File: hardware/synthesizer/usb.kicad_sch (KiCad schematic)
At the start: 6 parts, among them J8 USB_C_Receptacle_USB2.0_14P, U6 USBLC6-2P6

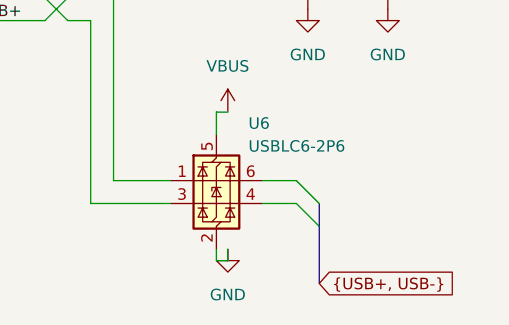
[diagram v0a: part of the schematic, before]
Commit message: start connecting sheets
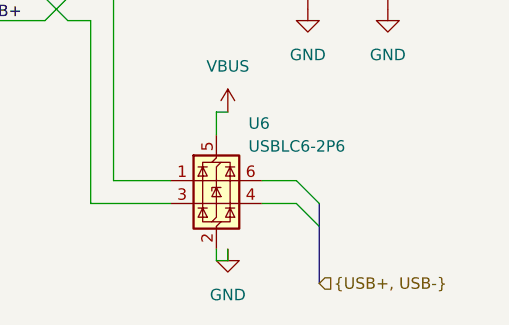
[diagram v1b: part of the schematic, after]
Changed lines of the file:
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@@
 		)
 	)
-	(global_label "{USB+, USB-}"
+	(hierarchical_label "{USB+, USB-}"
 		(shape input)
 		(at 152.4 114.3 0)
-		(fields_autoplaced yes)
 		(effects
 			(font
@@
 			(justify left)
 		)
-		(property "Intersheetrefs" "${INTERSHEET_REFS}"
-			(at 169.4158 114.3 0)
-			(effects
-				(font
-					(size 1.27 1.27)
-				)
-				(justify left)
-				(hide yes)
-			)
-		)
 	)

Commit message: update synthesizer
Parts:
- removed D2: D, Diode_SMD:D_0201_0603Metric, symbol Device:D
- added D?: 5.0V, symbol Device:D_Schottky
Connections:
- net GND: now also D?.2 (A)
- net VBUS: now also F2.2, D?.1 (K)
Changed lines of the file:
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@@
 	(paper "A4")
+	(junction
+		(at 133.35 60.96)
+		(diameter 0)
+		(color 0 0 0 0)
+	)
 	(junction
 		(at 114.3 85.09)
@@
 	(wire
 		(pts
+			(xy 124.46 60.96) (xy 124.46 67.31)
+		)
+		(stroke
+			(width 0)
+			(type default)
+		)
+	)
+	(wire
+		(pts
 			(xy 124.46 82.55) (xy 129.54 82.55)
 		)
@@
 	(wire
 		(pts
+			(xy 124.46 60.96) (xy 133.35 60.96)
+		)
+		(stroke
+			(width 0)
+			(type default)
+		)
+	)
+	(wire
+		(pts
 			(xy 113.03 85.09) (xy 114.3 85.09)
 		)
@@
 	(wire
 		(pts
-			(xy 128.27 67.31) (xy 133.35 67.31)
-		)
-		(stroke
-			(width 0)
-			(type default)
-		)
-	)
-	(wire
-		(pts
 			(xy 129.54 102.87) (xy 135.89 102.87)
 		)
@@
 	(wire
 		(pts
+			(xy 133.35 60.96) (xy 137.16 60.96)
+		)
+		(stroke
+			(width 0)
+			(type default)
+		)
+	)
+	(wire
+		(pts
 			(xy 151.13 74.93) (xy 151.13 76.2)
 		)
@@
 		(pts
 			(xy 124.46 85.09) (xy 127 85.09)
+		)
+		(stroke
+			(width 0)
+			(type default)
+		)
+	)
+	(wire
+		(pts
+			(xy 120.65 67.31) (xy 124.46 67.31)
 		)
 		(stroke
@@
 	)
 	(hierarchical_label "{USB+, USB-}"
-		(shape input)
+		(shape output)
 		(at 152.4 114.3 0)
 		(effects
@@
 	)
 	(symbol
+		(lib_id "Device:D_Schottky")
+		(at 133.35 64.77 270)
+		(unit 1)
+		(exclude_from_sim no)
+		(in_bom yes)
+		(on_board yes)
+		(dnp no)
+		(fields_autoplaced yes)
+		(property "Reference" "D?"
+			(at 135.89 63.1824 90)
+			(effects
+				(font
+					(size 1.27 1.27)
+				)
+				(justify left)
+			)
+		)
+		(property "Value" "5.0V"
+			(at 135.89 65.7224 90)
+			(effects
+				(font
+					(size 1.27 1.27)
+				)
+				(justify left)
+			)
+		)
+		(property "Footprint" ""
+			(at 133.35 64.77 0)
+			(effects
+				(font
+					(size 1.27 1.27)
+				)
+				(hide yes)
+			)
+		)
+		(property "Datasheet" "~"
+			(at 133.35 64.77 0)
+			(effects
+				(font
+					(size 1.27 1.27)
+				)
+				(hide yes)
+			)
+		)
+		(property "Description" "Schottky diode"
+			(at 133.35 64.77 0)
+			(effects
+				(font
+					(size 1.27 1.27)
+				)
+				(hide yes)
+			)
+		)
+		(pin "1"
+		)
+		(pin "2"
+		)
+		(instances
+			(project ""
+				(path "/f8740766-88d0-4c4d-b661-742f36f22c7b/70b9532c-c710-4ea4-8ea8-ed8989840f51"
+					(reference "D?")
+					(unit 1)
+				)
+			)
+		)
+	)
+	(symbol
 		(lib_id "Device:R")
 		(at 151.13 80.01 180)
@@
 	)
 	(symbol
+		(lib_id "power:GND")
+		(at 133.35 68.58 0)
+		(unit 1)
+		(exclude_from_sim no)
+		(in_bom yes)
+		(on_board yes)
+		(dnp no)
+		(property "Reference" "#PWR018"
+			(at 133.35 74.93 0)
+			(effects
+				(font
+					(size 1.27 1.27)
+				)
+				(hide yes)
+			)
+		)
+		(property "Value" "GND"
+			(at 136.398 70.612 0)
+			(effects
+				(font
+					(size 1.27 1.27)
+				)
+			)
+		)
+		(property "Footprint" ""
+			(at 133.35 68.58 0)
+			(effects
+				(font
+					(size 1.27 1.27)
+				)
+				(hide yes)
+			)
+		)
+		(property "Datasheet" ""
+			(at 133.35 68.58 0)
+			(effects
+				(font
+					(size 1.27 1.27)
+				)
+				(hide yes)
+			)
+		)
+		(property "Description" "Power symbol creates a global label with name \"GND\" , ground"
+			(at 133.35 68.58 0)
+			(effects
+				(font
+					(size 1.27 1.27)
+				)
+				(hide yes)
+			)
+		)
+		(pin "1"
+		)
+		(instances
+			(project ""
+				(path "/f8740766-88d0-4c4d-b661-742f36f22c7b/70b9532c-c710-4ea4-8ea8-ed8989840f51"
+					(reference "#PWR018")
+					(unit 1)
+				)
+			)
+		)
+	)
+	(symbol
 		(lib_id "Connector:USB_C_Receptacle_USB2.0_14P")
 		(at 97.79 82.55 0)
@@
 	)
 	(symbol
-		(lib_id "Device:D")
-		(at 124.46 67.31 180)
-		(unit 1)
-		(exclude_from_sim no)
-		(in_bom yes)
-		(on_board yes)
-		(dnp no)
-		(fields_autoplaced yes)
-		(property "Reference" "D2"
-			(at 124.46 60.96 0)
-			(effects
-				(font
-					(size 1.27 1.27)
-				)
-			)
-		)
-		(property "Value" "D"
-			(at 124.46 63.5 0)
-			(effects
-				(font
-					(size 1.27 1.27)
-				)
-			)
-		)
-		(property "Footprint" "Diode_SMD:D_0201_0603Metric"
-			(at 124.46 67.31 0)
-			(effects
-				(font
-					(size 1.27 1.27)
-				)
-				(hide yes)
-			)
-		)
-		(property "Datasheet" "~"
-			(at 124.46 67.31 0)
-			(effects
-				(font
-					(size 1.27 1.27)
-				)
-				(hide yes)
-			)
-		)
-		(property "Description" "Diode"
-			(at 124.46 67.31 0)
-			(effects
-				(font
-					(size 1.27 1.27)
-				)
-				(hide yes)
-			)
-		)
-		(property "Sim.Device" "D"
-			(at 124.46 67.31 0)
-			(effects
-				(font
-					(size 1.27 1.27)
-				)
-				(hide yes)
-			)
-		)
-		(property "Sim.Pins" "1=K 2=A"
-			(at 124.46 67.31 0)
-			(effects
-				(font
-					(size 1.27 1.27)
-				)
-				(hide yes)
-			)
-		)
-		(pin "1"
-		)
-		(pin "2"
-		)
-		(instances
-			(project "synthesizer"
-				(path "/f8740766-88d0-4c4d-b661-742f36f22c7b/70b9532c-c710-4ea4-8ea8-ed8989840f51"
-					(reference "D2")
-					(unit 1)
-				)
-			)
-		)
-	)
-	(symbol
 		(lib_id "power:VBUS")
-		(at 133.35 67.31 0)
+		(at 137.16 60.96 0)
 		(unit 1)
 		(exclude_from_sim no)
@@
 		(fields_autoplaced yes)
 		(property "Reference" "#PWR07"
-			(at 133.35 71.12 0)
+			(at 137.16 64.77 0)
 			(effects
 				(font
@@
 		)
 		(property "Value" "VBUS"
-			(at 133.35 62.23 0)
+			(at 137.16 55.88 0)
 			(effects
 				(font
@@
 		)
 		(property "Footprint" ""
-			(at 133.35 67.31 0)
+			(at 137.16 60.96 0)
 			(effects
 				(font
@@
 		)
 		(property "Datasheet" ""
-			(at 133.35 67.31 0)
+			(at 137.16 60.96 0)
 			(effects
 				(font
@@
 		)
 		(property "Description" "Power symbol creates a global label with name \"VBUS\""
-			(at 133.35 67.31 0)
-			(effects
-				(font
+			(at 137.16 60.96 0)
+			(effects
+				(font

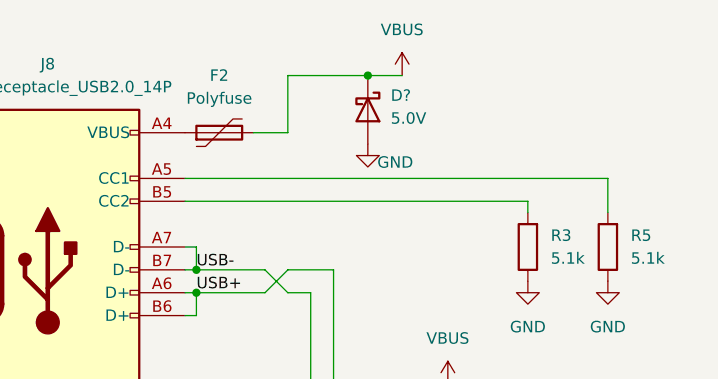
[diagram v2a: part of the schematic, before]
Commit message: finish ethernet jack
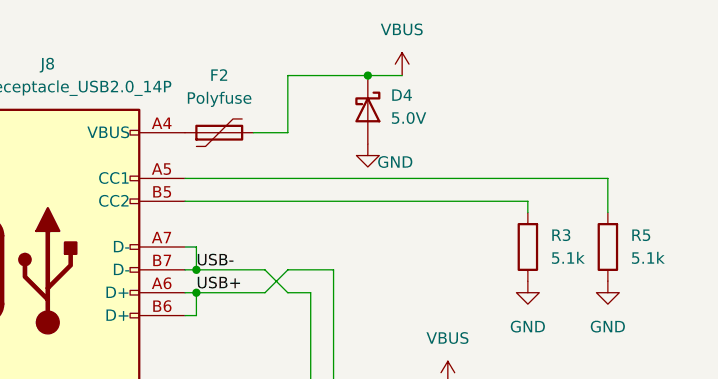
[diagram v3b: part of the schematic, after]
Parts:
- gave numbers to parts that had none: 1
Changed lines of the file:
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@@
 		(dnp no)
 		(fields_autoplaced yes)
-		(property "Reference" "D?"
+		(property "Reference" "D4"
 			(at 135.89 63.1824 90)
 			(effects
@@
 			(project ""
 				(path "/f8740766-88d0-4c4d-b661-742f36f22c7b/70b9532c-c710-4ea4-8ea8-ed8989840f51"
-					(reference "D?")
+					(reference "D4")
 					(unit 1)
 				)

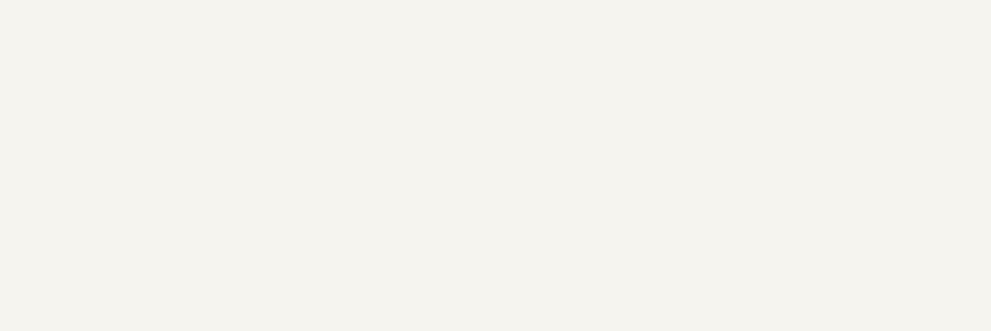
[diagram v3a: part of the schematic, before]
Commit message: add logo to every sheet
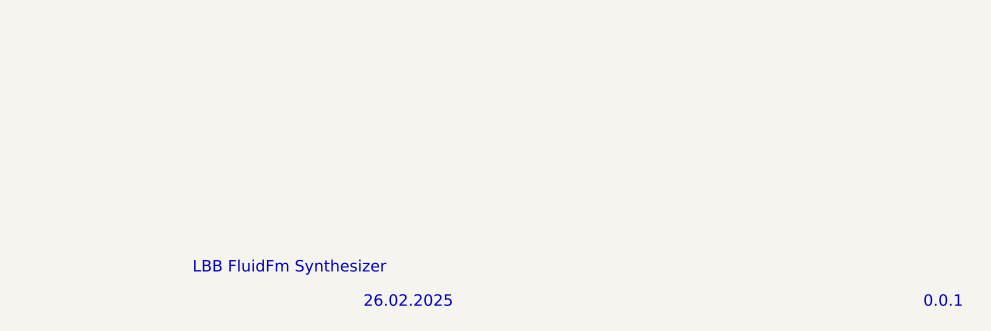
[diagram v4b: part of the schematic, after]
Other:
- note added: "0.0.1"
- note added: "26.02.2025"
- note added: "LBB FluidFm Synthesizer"

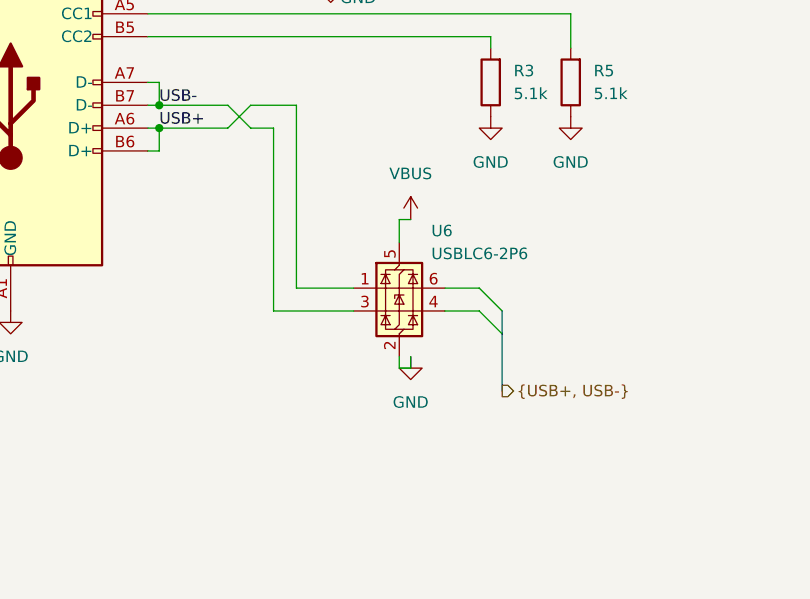
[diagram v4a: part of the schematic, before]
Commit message: work on synthesizer schematics - add HSE and LSE oscillators
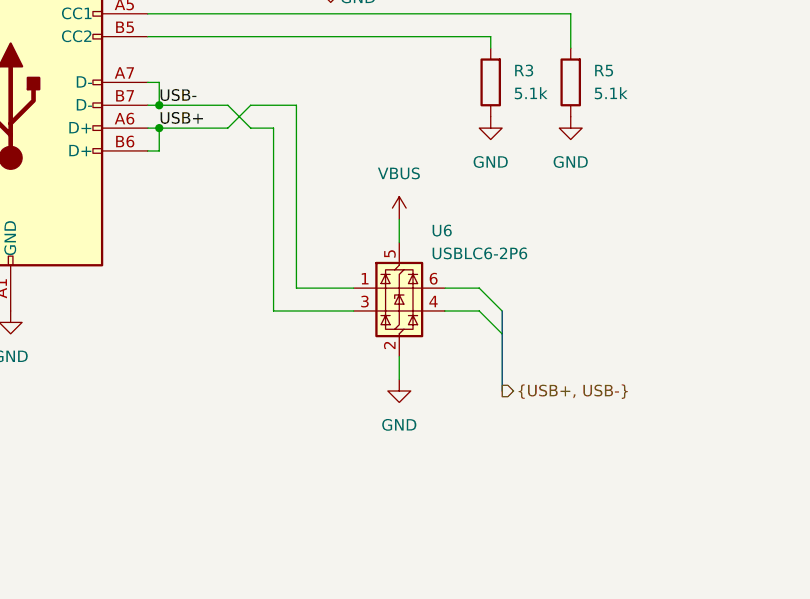
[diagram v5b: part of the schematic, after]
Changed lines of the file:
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@@
-	(wire
-		(pts
-			(xy 140.97 111.76) (xy 142.24 111.76)
-		)
-		(stroke
-			(width 0)
-			(type default)
-		)
-	)
 	(wire
 		(pts
@@
 	(wire
 		(pts
-			(xy 140.97 95.25) (xy 142.24 95.25)
-		)
-		(stroke
-			(width 0)
-			(type default)
-		)
-	)
-	(wire
-		(pts
 			(xy 114.3 85.09) (xy 114.3 87.63)
 		)
@@
 	(wire
 		(pts
-			(xy 140.97 110.49) (xy 140.97 111.76)
-		)
-		(stroke
-			(width 0)
-			(type default)
-		)
-	)
-	(wire
-		(pts
-			(xy 142.24 111.76) (xy 142.24 110.49)
-		)
-		(stroke
-			(width 0)
-			(type default)
-		)
-	)
-	(wire
-		(pts
 			(xy 146.05 105.41) (xy 149.86 105.41)
 		)
@@
 		(pts
 			(xy 152.4 107.95) (xy 152.4 114.3)
+		)
+		(stroke
+			(width 0)
+			(type default)
+		)
+	)
+	(wire
+		(pts
+			(xy 140.97 110.49) (xy 140.97 113.03)
 		)
 		(stroke
@@
 			"IgBmAGoAZQBVAHUAWQBNAHAAVQAvAFAAVwBGAHEALwB3AFIANgBuAE0AUABlAE0AVwBXADEAMQBS"
 			"AFIASABrAGcAWgAzAFIAOQBaAFcATQBKAE0AUABjAG0AZwBZAFUAQQB0ADcAWABJAEkANgBGAGsA"
-			"NwBzAHMAcA=="
+			"NwBzAHMAcFRVd0JhaDVMQUNkQWJLejYydm9vckNpelptVmpIMjgrbHpvcUR1aUIrRFcrY0IwVkFD"
+			"Y2syR0lrSGtFREZZWEI1RmU5NTgvQzhiOEs2bFozMDNzdjZ3UlRvZHJPb0pDckFOeWlROXFERHFM"
+			"OFM0L2FyQnhiRjJNN3Jza0VhTHdCVEc4ZDhLaEg4eVVMZFNHWGtmSktsM0o0QWdzZEZ5NEEvM2x5"
+			"bGk1WkZTOHBORGxVY0tTdElORU50dE5mcE9JQ2tvV1JuOUExZUJPclk5R1ZKc0dtWjR0TWJPMm1v"
+			"czFqc2FaYVgvZFpiMXdHZUE0a05BWlFVTXI1T29RSGFxSVg1UjI4LzU1VGY1dyt1WFlmdVNzbW9k"
+			"MFVEK1ZnQjBic0U3dVVHTWVtTCtzdTQ5ZktoUmRuMFAzOVdxUHN6Mm1uM3FkcmhxeCt1L1RlZ3NJ"
+			"U0FUa2U0YlYwWnYzWnV4NUtOZlRmMkVCekZFR25YM0UvYmJwVGhHVUJrL3BMWUdGaEpQU3JPNC9v"
+			"MVZYeHdaSEVnc2RudS84aVZnOXZXcm9paFRoc0lrQW9ZZ2trRkF0aDRGcTRhWFlYM1hUWjR5amRq"
+			"dEs5S3QxODFaR0lmbFBJaEo4V2taU2hsL0RJQ3hWMDNYcmg0a1ZtSG81RnVoUHBmMjduUHVUa2Jm"
+			"azUyOUZuekZBQ1RZc3RLeHVjM1Zlbmk1VzVKRnpVdVh1NmdxQmxWUm51ZHR2OWlKVkJpMG9RS0Qw"
+			"L0FTSWZENzUxWDN2YTJzeGJQVnJLbjI5c1pQN0RqdG91TS96dUlUcUNJOGVSQUVnWWxyQ2d4N3Rv"
+			"KzlwcmY2bE8vT0VKYlJyb3pFakl0QUE5SkVFQVV6QXhvSForODlseThZYkJuVVRmLzIvdmp3Q0hl"
+			"M250ekg4NzVUMk9KQnVxTkdvTmlqSGFYOE50akVkNDlXRGtqS3RWWHJJaXA2aHdTMU5vR2NOb09R"
+			"Q0JrTS8xMUNDcE9jTXR3aE52WFY2bTM3QjVZekV1YjVmMHVHZWloTzI3YUFPT2VrRUtjbzFHeEVF"
+			"aUJPMi9lakhXOXA0YzYrT3ZiTGg0WjdLc2FDVnBSWWdOc25KVHYzSGdXUG5QdHlLSTdnUE82SEkx"
+			"MWxkQWVVSjJuRFdhTjFCenU2SWhSTFpmeG0yc2RiaCtMYWJnelBxUHU1bHRYeG9pazNINzRwKzIv"
+			"VWhXbEdGdFhBWi9mM0VXdE1zRDJLdTk5MitYOTlPR3JoZ05wUDJCMVJ3RWFJV05CTm96VXhtb042"
+			"Y25JeHYzSlpUSnYrUWRSUXhrbWlGZ0hUaHRTNE82YkxzVDFtMWFkOWsxWlVTM3Qvb2NQYkVKUHRa"
+			"d2hjU3pORA=="
 		)
 	)
@@
 			"AAAAAgAAAAAAAAAAAAAAAAAAAAAAAAAAAAAAAAAAAAAAAAAAAAAAAAAAAAAAAAAAAAAAAAAAAAAA"
 			"AAAAAAAAAAAAAAAAAAAAAAAAAAAAAAAAAAAAAAAAAAAAAAAAAAAAAAAAAAAAAAAAAAAAAAAAAAAA"
-			"AAAAAAAAAAAAAAAAAAAAAAAAAAAAAAAAAAAAAAAAAAAAAAAAAAAAAAAAAAAAAAAAAA=="
+			"AAAAAAAAAAAAAAAAAAAAAAAAAAAAAAAAAAAAAAAAAAAAAAAAAAAAAAAAAAAAAAAAAGZkOGZmZTAw"
+			"MDEwNGE0NjQ5NDYwMDAxMDEwMDAwMDEwMDAxMDAwMGZmZGIwMDQzMDAwOAowNjA2MDcwNjA1MDgw"
+			"NzA3MDcwOTA5MDgwYTBjMTQwZDBjMGIwYjBjMTkxMjEzMGYxNDFkMWExZjFlMWQxYTFjMWMyMDI0"
+			"MmUKMjcyMDIyMmMyMzFjMWMyODM3MjkyYzMwMzEzNDM0MzQxZjI3MzkzZDM4MzIzYzJlMzMzNDMy"
+			"ZmZkYjAwNDMwMTA5MDkwOTBjCjBiMGMxODBkMGQxODMyMjExYzIxMzIzMjMyMzIzMjMyMzIzMjMy"
+			"MzIzMjMyMzIzMjMyMzIzMjMyMzIzMjMyMzIzMjMyMzIzMgozMjMyMzIzMjMyMzIzMjMyMzIzMjMy"
+			"MzIzMjMyMzIzMjMyMzIzMjMyMzIzMjMyMzJmZmMwMDAxMTA4MDA4OTAxMDAwMzAxMjIKMDAwMjEx"
+			"MDEwMzExMDFmZmM0MDAxZjAwMDAwMTA1MDEwMTAxMDEwMTAxMDAwMDAwMDAwMDAwMDAwMDAxMDIw"
+			"MzA0MDUwNjA3CjA4MDkwYTBiZmZjNDAwYjUxMDAwMDIwMTAzMDMwMjA0MDMwNTA1MDQwNDAwMDAw"
+			"MTdkMDEwMjAzMDAwNDExMDUxMjIxMzE0MQowNjEzNTE2MTA3MjI3MTE0MzI4MTkxYTEwODIzNDJi"
+			"MWMxMTU1MmQxZjAyNDMzNjI3MjgyMDkwYTE2MTcxODE5MWEyNTI2MjcKMjgyOTJhMzQzNTM2Mzcz"
+			"ODM5M2E0MzQ0NDU0NjQ3NDg0OTRhNTM1NDU1NTY1NzU4NTk1YTYzNjQ2NTY2Njc2ODY5NmE3Mzc0"
+			"Cjc1NzY3Nzc4Nzk3YTgzODQ4NTg2ODc4ODg5OGE5MjkzOTQ5NTk2OTc5ODk5OWFhMmEzYTRhNWE2"
+			"YTdhOGE5YWFiMmIzYjRiNQpiNmI3YjhiOWJhYzJjM2M0YzVjNmM3YzhjOWNhZDJkM2Q0ZDVkNmQ3"
+			"ZDhkOWRhZTFlMmUzZTRlNWU2ZTdlOGU5ZWFmMWYyZjMKZjRmNWY2ZjdmOGY5ZmFmZmM0MDAxZjAx"
+			"MDAwMzAxMDEwMTAxMDEwMTAxMDEwMTAwMDAwMDAwMDAwMDAxMDIwMzA0MDUwNjA3CjA4MDkwYTBi"
+			"ZmZjNDAwYjUxMTAwMDIwMTAyMDQwNDAzMDQwNzA1MDQwNDAwMDEwMjc3MDAwMTAyMDMxMTA0MDUy"
+			"MTMxMDYxMgo0MTUxMDc2MTcxMTMyMjMyODEwODE0NDI5MWExYjFjMTA5MjMzMzUyZjAxNTYyNzJk"
+			"MTBhMTYyNDM0ZTEyNWYxMTcxODE5MWEKMjYyNzI4MjkyYTM1MzYzNzM4MzkzYTQzNA=="
 		)
 	)
@@
 	(symbol
 		(lib_id "power:VBUS")
-		(at 142.24 95.25 0)
+		(at 140.97 95.25 0)
 		(unit 1)
 		(exclude_from_sim no)
@@
 		(fields_autoplaced yes)
 		(property "Reference" "#PWR028"
-			(at 142.24 99.06 0)
+			(at 140.97 99.06 0)
 			(effects
 				(font
@@
 		)
 		(property "Value" "VBUS"
-			(at 142.24 90.17 0)
+			(at 140.97 90.17 0)
 			(effects
 				(font
@@
 		)
 		(property "Footprint" ""
-			(at 142.24 95.25 0)
+			(at 140.97 95.25 0)
 			(effects
 				(font
@@
 		)
 		(property "Datasheet" ""
-			(at 142.24 95.25 0)
+			(at 140.97 95.25 0)
 			(effects
 				(font
@@
 		)
 		(property "Description" "Power symbol creates a global label with name \"VBUS\""
-			(at 142.24 95.25 0)
+			(at 140.97 95.25 0)
 			(effects
 				(font
@@
 	(symbol
 		(lib_id "power:GND")
-		(at 142.24 110.49 0)
+		(at 140.97 113.03 0)
 		(unit 1)
 		(exclude_from_sim no)
@@
 		(fields_autoplaced yes)
 		(property "Reference" "#PWR029"
-			(at 142.24 116.84 0)
+			(at 140.97 119.38 0)
 			(effects
 				(font
@@
 		)
 		(property "Value" "GND"
-			(at 142.24 115.57 0)
+			(at 140.97 118.11 0)
 			(effects
 				(font
@@
 		)
 		(property "Footprint" ""
-			(at 142.24 110.49 0)
+			(at 140.97 113.03 0)
 			(effects
 				(font
@@
 		)
 		(property "Datasheet" ""
-			(at 142.24 110.49 0)
+			(at 140.97 113.03 0)
 			(effects
 				(font
@@
 		)
 		(property "Description" "Power symbol creates a global label with name \"GND\" , ground"
-			(at 142.24 110.49 0)
-			(effects
-				(font
+			(at 140.97 113.03 0)
+			(effects
+				(font

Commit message: improved pcb design
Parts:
- J8: footprint (none) -> Connector_USB:USB_C_Receptacle_HCTL_HC-TYPE-C-16P-01A
- R3, R5: footprint (none) -> Resistor_SMD:R_0603_1608Metric
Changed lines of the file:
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@@
 			)
 		)
-		(property "Footprint" ""
+		(property "Footprint" "Resistor_SMD:R_0603_1608Metric"
 			(at 152.908 80.01 90)
 			(effects
@@
 			)
 		)
-		(property "Footprint" ""
+		(property "Footprint" "Resistor_SMD:R_0603_1608Metric"
 			(at 161.798 80.01 90)
 			(effects
@@
 			)
 		)
-		(property "Footprint" ""
+		(property "Footprint" "Connector_USB:USB_C_Receptacle_HCTL_HC-TYPE-C-16P-01A"
 			(at 101.6 82.55 0)
 			(effects
